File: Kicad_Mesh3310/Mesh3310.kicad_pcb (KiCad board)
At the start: 4 copper layers, 41.4 x 108 mm, 167 parts, among them J1 USB device, J2 Mic, J3 Sim, J4 Conn_01x05_Pin, J5 Vibrator, J6 Buzzer, J7 Display, J9 Battery, Q4 BSS138, Q5 BSS138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

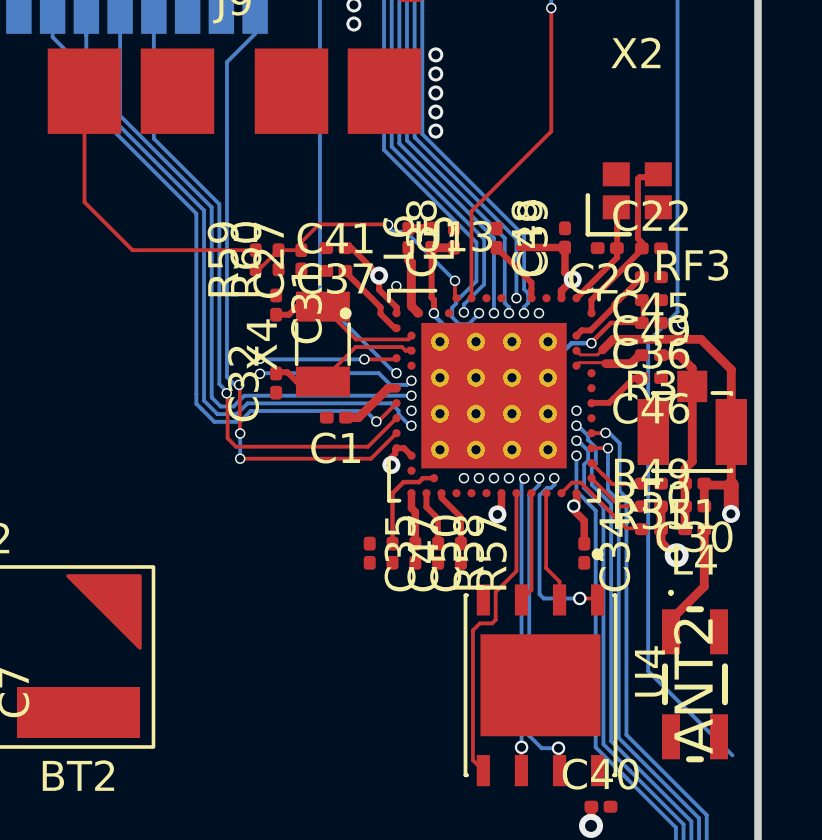
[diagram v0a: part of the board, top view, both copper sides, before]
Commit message: shematic changes
small changes in NRF component
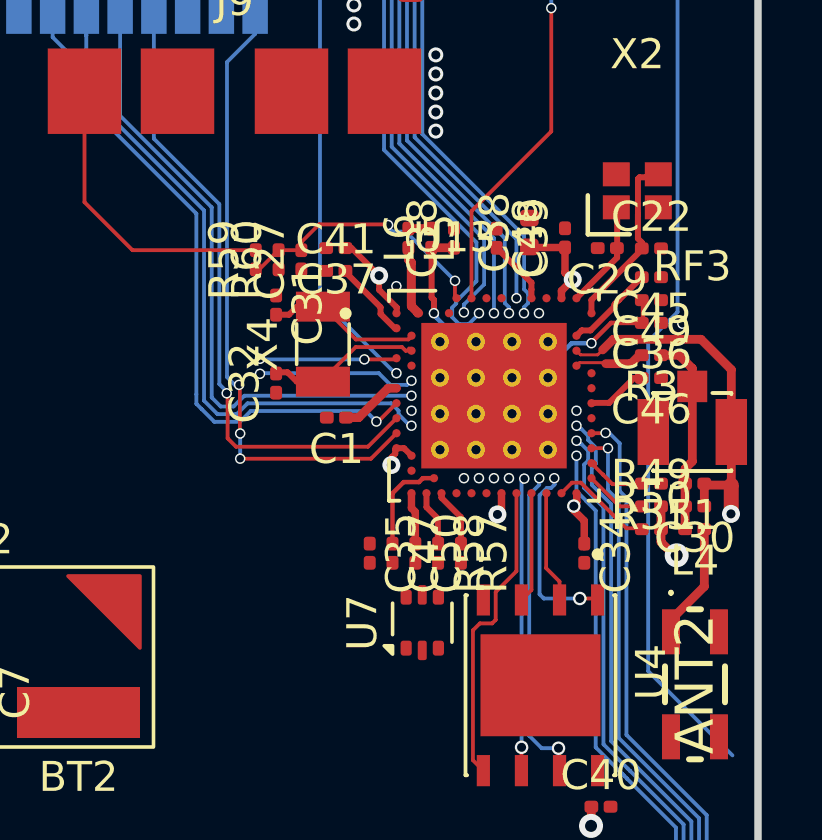
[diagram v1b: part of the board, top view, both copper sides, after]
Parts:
- added C58: 100nF, Capacitor_SMD:C_0402_1005Metric, F.Cu at (153.8, 69.9)
- added U7: USBLC6-2P6, Package_TO_SOT_SMD:SOT-666, F.Cu at (150.2, 82.9)
- C22, C29: value 10pF -> 18pF
- C31, C32: value 10nF -> 12pF
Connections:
- R57 pad 2: /USB_D+ -> /MCU/DIODE_USB_D+
- R58 pad 2: /USB_D- -> /MCU/DIODE_USB_D-
